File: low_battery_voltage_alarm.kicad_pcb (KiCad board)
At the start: 2 copper layers, 88.9 x 53.3 mm, 27 parts, among them J1 V-DISPLAY, Q1 2N4401, Q2 2N4401, SW1 SW_DIP_x01, U1 NE555P

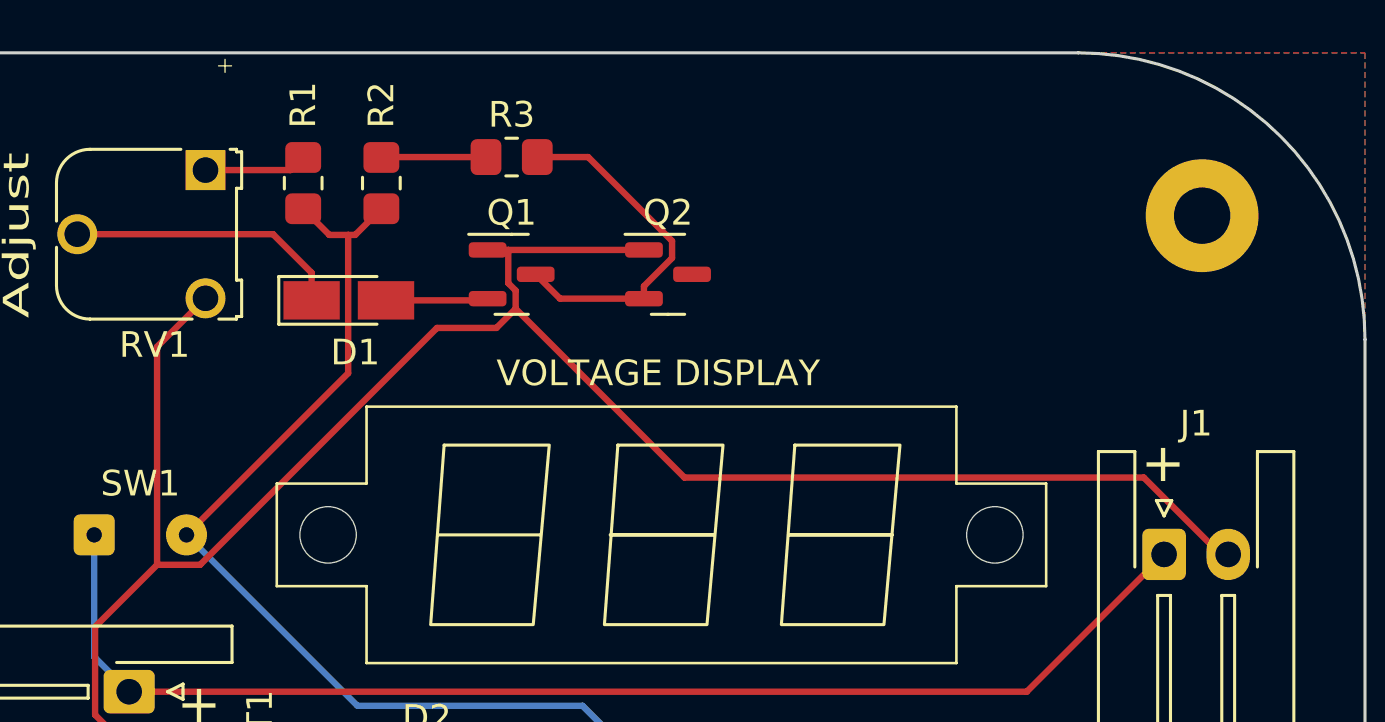
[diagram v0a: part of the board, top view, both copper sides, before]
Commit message: change 2N4401 => MMBT4401
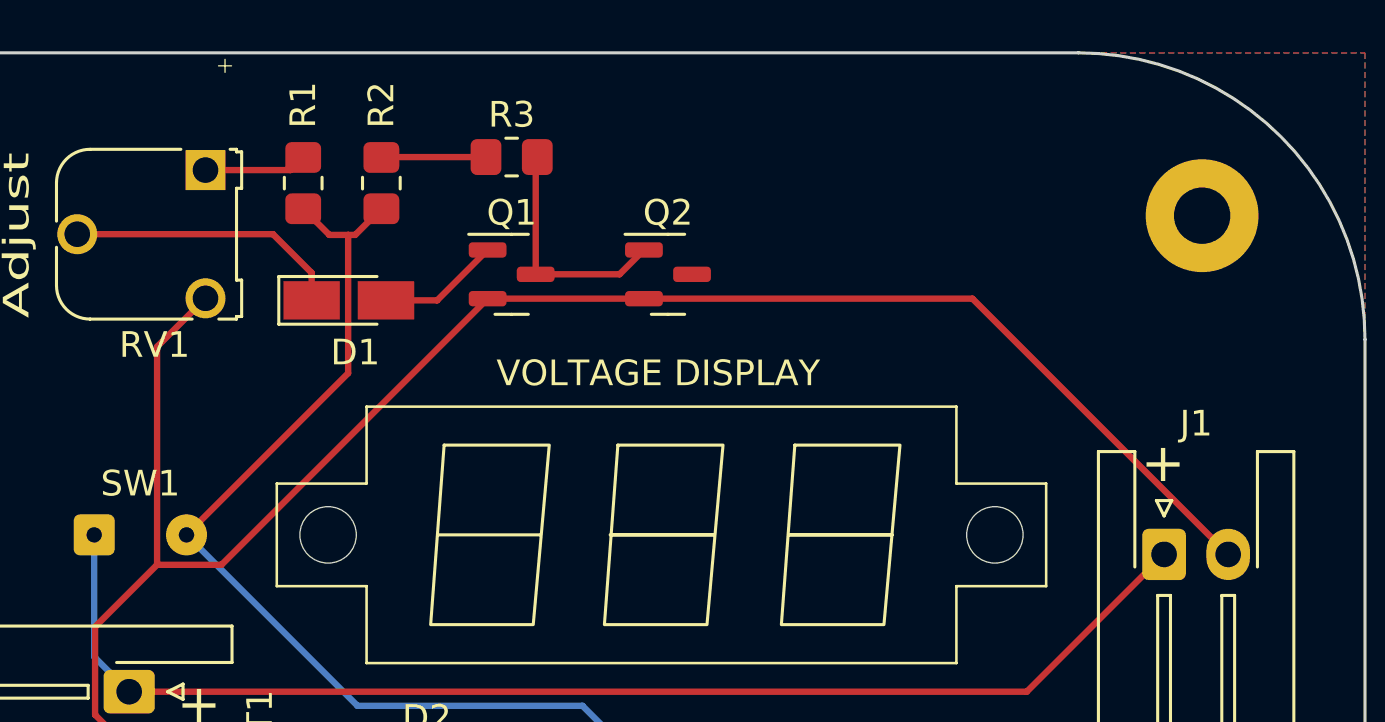
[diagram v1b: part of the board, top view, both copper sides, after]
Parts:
- Q1, Q2: value 2N4401 -> MMBT4401
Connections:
- Q1 pad 1: Net-(BT1-Pad2) -> Net-(D1-Pad2)
- Q1 pad 2: Net-(D1-Pad2) -> Net-(BT1-Pad2)
- Q1 pad 3: Net-(Q1-Pad3) -> Net-(Q2-Pad1)
- Q2 pad 1: Net-(BT1-Pad2) -> Net-(Q2-Pad1)
- Q2 pad 2: Net-(Q1-Pad3) -> Net-(BT1-Pad2)
- R3 pad 2: Net-(Q1-Pad3) -> Net-(Q2-Pad1)
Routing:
- net Net-(Q1-Pad3): track 13.9 -> 0.00 mm
- net Net-(Q2-Pad1): track 0.00 -> 9.21 mm
- net Net-(BT1-Pad2): track 79.1 -> 70.9 mm
- net Net-(D1-Pad2): track 3.99 -> 4.78 mm
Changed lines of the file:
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@@
   (net 9 "Net-(D1-Pad2)")
   (net 10 "Net-(D2-Pad2)")
-  (net 11 "Net-(Q1-Pad3)")
+  (net 11 "Net-(Q2-Pad1)")
   (net 12 "Net-(R1-Pad2)")
   (net 13 "Net-(R2-Pad2)")
@@
       (effects (font (size 1 1) (thickness 0.15)))
     )
-    (fp_text value "2N4401" (at 0 2.4) (layer "F.Fab")
+    (fp_text value "MMBT4401" (at 0 2.4) (layer "F.Fab")
       (effects (font (size 1 1) (thickness 0.15)))
     )
@@
     (fp_line (start 0.65 -1.45) (end 0.65 1.45) (layer "F.Fab") (width 0.1))
     (pad "1" smd roundrect (at -0.9375 -0.95) (size 1.475 0.6) (layers "F.Cu" "F.Paste" "F.Mask") (roundrect_rratio 0.25)
+      (net 9 "Net-(D1-Pad2)") (pinfunction "B") (pintype "input"))
+    (pad "2" smd roundrect (at -0.9375 0.95) (size 1.475 0.6) (layers "F.Cu" "F.Paste" "F.Mask") (roundrect_rratio 0.25)
       (net 2 "Net-(BT1-Pad2)") (pinfunction "E") (pintype "passive"))
-    (pad "2" smd roundrect (at -0.9375 0.95) (size 1.475 0.6) (layers "F.Cu" "F.Paste" "F.Mask") (roundrect_rratio 0.25)
-      (net 9 "Net-(D1-Pad2)") (pinfunction "B") (pintype "passive"))
     (pad "3" smd roundrect (at 0.9375 0) (size 1.475 0.6) (layers "F.Cu" "F.Paste" "F.Mask") (roundrect_rratio 0.25)
-      (net 11 "Net-(Q1-Pad3)") (pinfunction "C") (pintype "passive"))
+      (net 11 "Net-(Q2-Pad1)") (pinfunction "C") (pintype "passive"))
     (model "${KICAD6_3DMODEL_DIR}/Package_TO_SOT_SMD.3dshapes/SOT-23.wrl"
       (offset (xyz 0 0 0))
@@
       (effects (font (size 1 1) (thickness 0.15)))
     )
-    (fp_text value "2N4401" (at 0 2.4) (layer "F.Fab")
+    (fp_text value "MMBT4401" (at 0 2.4) (layer "F.Fab")
       (effects (font (size 1 1) (thickness 0.15)))
     )
@@
     (fp_line (start 0.65 1.45) (end -0.65 1.45) (layer "F.Fab") (width 0.1))
     (pad "1" smd roundrect (at -0.9375 -0.95) (size 1.475 0.6) (layers "F.Cu" "F.Paste" "F.Mask") (roundrect_rratio 0.25)
+      (net 11 "Net-(Q2-Pad1)") (pinfunction "B") (pintype "input"))
+    (pad "2" smd roundrect (at -0.9375 0.95) (size 1.475 0.6) (layers "F.Cu" "F.Paste" "F.Mask") (roundrect_rratio 0.25)
       (net 2 "Net-(BT1-Pad2)") (pinfunction "E") (pintype "passive"))
-    (pad "2" smd roundrect (at -0.9375 0.95) (size 1.475 0.6) (layers "F.Cu" "F.Paste" "F.Mask") (roundrect_rratio 0.25)
-      (net 11 "Net-(Q1-Pad3)") (pinfunction "B") (pintype "passive"))
     (pad "3" smd roundrect (at 0.9375 0) (size 1.475 0.6) (layers "F.Cu" "F.Paste" "F.Mask") (roundrect_rratio 0.25)
       (net 6 "GNDREF") (pinfunction "C") (pintype "passive"))
@@
       (net 13 "Net-(R2-Pad2)") (pintype "passive"))
     (pad "2" smd roundrect (at 1 0) (size 1.2 1.4) (layers "F.Cu" "F.Paste" "F.Mask") (roundrect_rratio 0.2083333333)
-      (net 11 "Net-(Q1-Pad3)") (pintype "passive"))
+      (net 11 "Net-(Q2-Pad1)") (pintype "passive"))
     (model "${KICAD6_3DMODEL_DIR}/Resistor_SMD.3dshapes/R_0805_2012Metric.wrl"
       (offset (xyz 0 0 0))
@@
   (segment (start 127.486 94.414) (end 128.85 95.778) (width 0.25) (layer "B.Cu") (net 1))
   (segment (start 127.486 89.662) (end 127.486 94.414) (width 0.25) (layer "B.Cu") (net 1))
-  (segment (start 143.6322 78.552) (end 142.8265 78.552) (width 0.25) (layer "F.Cu") (net 2))
-  (segment (start 171.4102 90.424) (end 171.704 90.424) (width 0.25) (layer "F.Cu") (net 2))
-  (segment (start 143.6322 79.847) (end 143.9196 80.1344) (width 0.25) (layer "F.Cu") (net 2))
+  (segment (start 142.8265 80.452) (end 148.9225 80.452) (width 0.25) (layer "F.Cu") (net 2))
   (segment (start 127.5218 93.2455) (end 127.5218 96.6807) (width 0.25) (layer "F.Cu") (net 2))
-  (segment (start 143.9196 80.1344) (end 143.9196 80.8445) (width 0.25) (layer "F.Cu") (net 2))
-  (segment (start 168.4134 87.4272) (end 171.4102 90.424) (width 0.25) (layer "F.Cu") (net 2))
-  (segment (start 150.5023 87.4272) (end 168.4134 87.4272) (width 0.25) (layer "F.Cu") (net 2))
-  (segment (start 148.9225 78.552) (end 143.6322 78.552) (width 0.25) (layer "F.Cu") (net 2))
+  (segment (start 161.732 80.452) (end 171.704 90.424) (width 0.25) (layer "F.Cu") (net 2))
   (segment (start 127.5218 96.6807) (end 127.9438 97.1027) (width 0.25) (layer "F.Cu") (net 2))
+  (segment (start 132.4495 90.829) (end 129.9383 90.829) (width 0.25) (layer "F.Cu") (net 2))
+  (segment (start 161.732 80.452) (end 148.9225 80.452) (width 0.25) (layer "F.Cu") (net 2))
   (segment (start 128.85 98.278) (end 128.85 97.1027) (width 0.25) (layer "F.Cu") (net 2))
   (segment (start 129.9383 90.829) (end 127.5218 93.2455) (width 0.25) (layer "F.Cu") (net 2))
-  (segment (start 143.6322 78.552) (end 143.6322 79.847) (width 0.25) (layer "F.Cu") (net 2))
   (segment (start 129.9383 82.3257) (end 129.9383 90.829) (width 0.25) (layer "F.Cu") (net 2))
   (segment (start 127.9438 97.1027) (end 128.85 97.1027) (width 0.25) (layer "F.Cu") (net 2))
-  (segment (start 143.9196 80.8445) (end 143.1707 81.5934) (width 0.25) (layer "F.Cu") (net 2))
   (segment (start 131.826 80.438) (end 129.9383 82.3257) (width 0.25) (layer "F.Cu") (net 2))
-  (segment (start 143.9196 80.8445) (end 150.5023 87.4272) (width 0.25) (layer "F.Cu") (net 2))
-  (segment (start 140.8531 81.5934) (end 131.6175 90.829) (width 0.25) (layer "F.Cu") (net 2))
-  (segment (start 143.1707 81.5934) (end 140.8531 81.5934) (width 0.25) (layer "F.Cu") (net 2))
-  (segment (start 131.6175 90.829) (end 129.9383 90.829) (width 0.25) (layer "F.Cu") (net 2))
+  (segment (start 142.8265 80.452) (end 132.4495 90.829) (width 0.25) (layer "F.Cu") (net 2))
   (segment (start 137.668 109.506) (end 140.494 106.68) (width 0.25) (layer "F.Cu") (net 3))
   (segment (start 137.668 114.3) (end 137.668 109.506) (width 0.25) (layer "F.Cu") (net 3))
@@
   (segment (start 135.964 80.518) (end 135.964 79.4427) (width 0.25) (layer "F.Cu") (net 8))
   (segment (start 126.826 77.938) (end 134.4593 77.938) (width 0.25) (layer "F.Cu") (net 8))
-  (segment (start 138.864 80.518) (end 142.7605 80.518) (width 0.25) (layer "F.Cu") (net 9))
-  (segment (start 142.7605 80.518) (end 142.8265 80.452) (width 0.25) (layer "F.Cu") (net 9))
+  (segment (start 138.864 80.518) (end 140.8605 80.518) (width 0.25) (layer "F.Cu") (net 9))
+  (segment (start 140.8605 80.518) (end 142.8265 78.552) (width 0.25) (layer "F.Cu") (net 9))
   (segment (start 141.727 102.907) (end 140.494 104.14) (width 0.25) (layer "F.Cu") (net 10))
   (segment (start 141.727 99.06) (end 141.727 102.907) (width 0.25) (layer "F.Cu") (net 10))
-  (segment (start 144.764 74.93) (end 146.7474 74.93) (width 0.25) (layer "F.Cu") (net 11))
-  (segment (start 148.9225 79.9645) (end 148.9225 80.452) (width 0.25) (layer "F.Cu") (net 11))
-  (segment (start 150.0194 78.202) (end 150.0194 78.8676) (width 0.25) (layer "F.Cu") (net 11))
-  (segment (start 148.9225 80.452) (end 145.6515 80.452) (width 0.25) (layer "F.Cu") (net 11))
-  (segment (start 145.6515 80.452) (end 144.7015 79.502) (width 0.25) (layer "F.Cu") (net 11))
-  (segment (start 150.0194 78.8676) (end 148.9225 79.9645) (width 0.25) (layer "F.Cu") (net 11))
-  (segment (start 146.7474 74.93) (end 150.0194 78.202) (width 0.25) (layer "F.Cu") (net 11))
+  (segment (start 147.9725 79.502) (end 148.9225 78.552) (width 0.25) (layer "F.Cu") (net 11))
+  (segment (start 144.7015 79.502) (end 144.7015 74.9925) (width 0.25) (layer "F.Cu") (net 11))
+  (segment (start 144.7015 79.502) (end 147.9725 79.502) (width 0.25) (layer "F.Cu") (net 11))
+  (segment (start 144.7015 74.9925) (end 144.764 74.93) (width 0.25) (layer "F.Cu") (net 11))
   (segment (start 131.826 75.438) (end 135.144 75.438) (width 0.25) (layer "F.Cu") (net 12))
   (segment (start 135.144 75.438) (end 135.636 74.946) (width 0.25) (layer "F.Cu") (net 12))

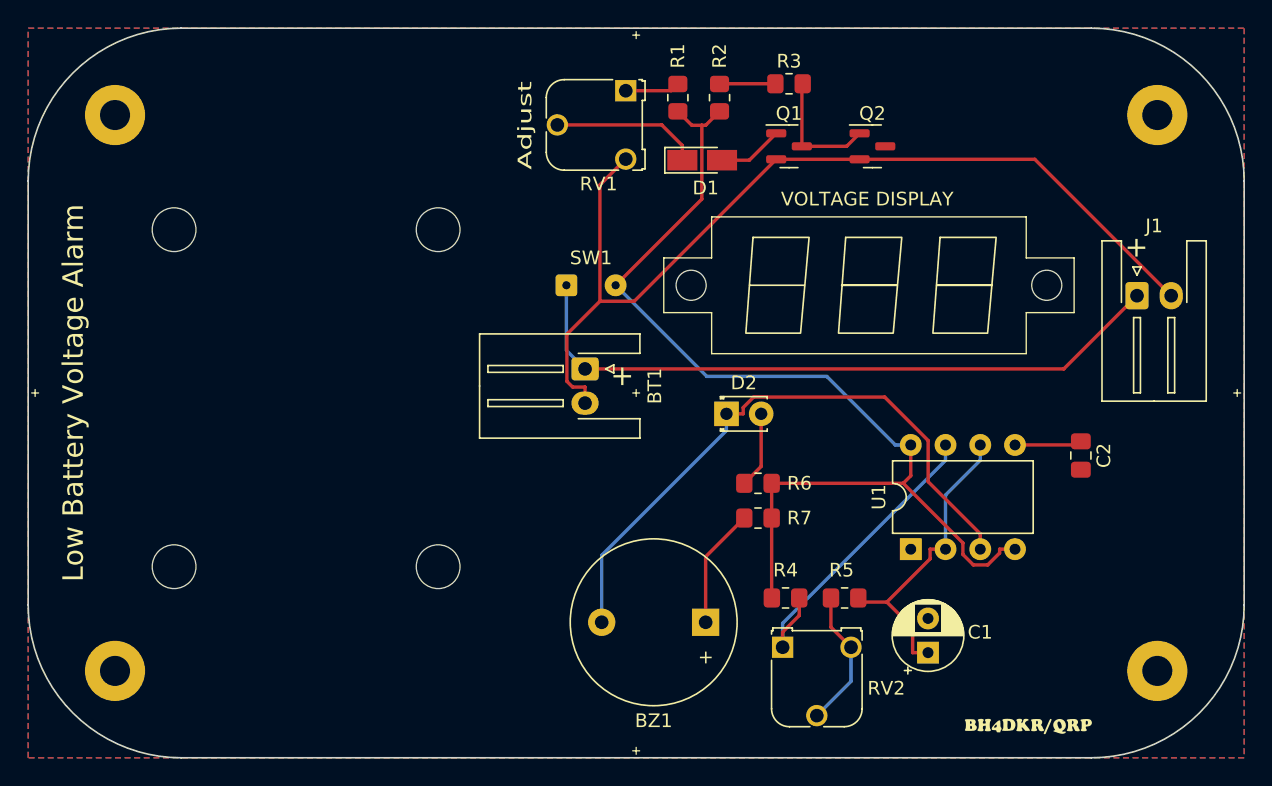
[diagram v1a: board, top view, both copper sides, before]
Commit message: change footprint error and add jumper to buzzer(mini power)
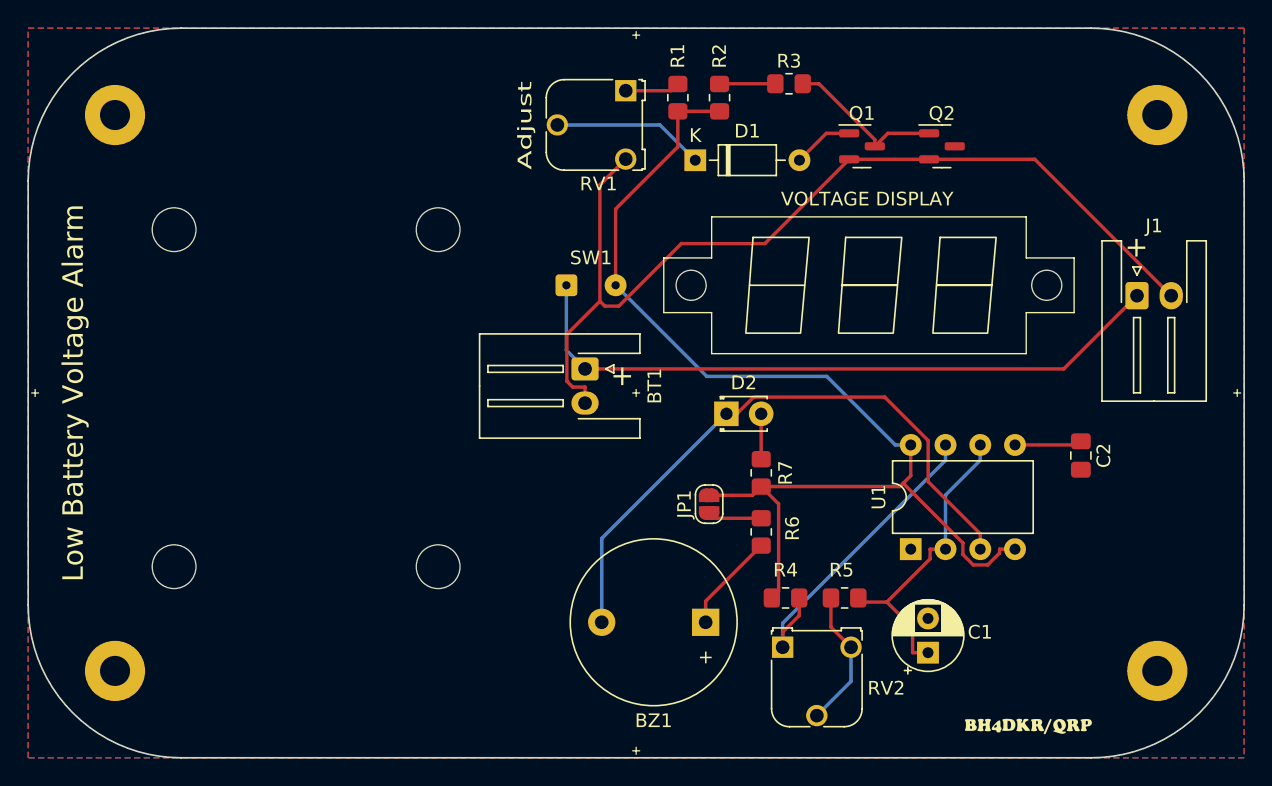
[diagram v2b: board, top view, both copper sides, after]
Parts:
- added JP1: EN_Buzzer, Jumper:SolderJumper-2_P1.3mm_Open_RoundedPad1.0x1.5mm, F.Cu at (137.9, 105.7)
- D1: footprint Diode_SMD:D_MicroMELF_Handsoldering -> Diode_THT:D_DO-35_SOD27_P7.62mm_Horizontal
- moved Q1 5.33 mm to (149.1, 79.5)
- moved Q2 5.08 mm to (154.9, 79.5)
- moved R7 1.04 mm to (141.7, 107.7), turned to 90 degrees
- moved R6 0.80 mm to (141.7, 103.4), turned to -90 degrees
- moved D1 0.51 mm to (136.9, 80.5)
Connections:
- R7 pad 2: Net-(R1-Pad1) -> Net-(R7-Pad2)
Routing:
- net Net-(R1-Pad1): track 77.4 -> 82.3 mm
- net Net-(R7-Pad2): track 0.00 -> 3.97 mm
- net Net-(Q1-Pad3): track 9.21 -> 11.8 mm
- net Net-(D2-Pad2): track 5.59 -> 3.32 mm
- net Net-(BZ1-Pad1): track 8.79 -> 7.29 mm
